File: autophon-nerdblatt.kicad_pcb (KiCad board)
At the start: 2 copper layers, 265 x 140 mm, 91 parts, among them J101 board-edge-connector, Q300 BSS84, Q301 BSS84, Q302 BSS84, Q303 BSS84, Q304 BSS84, Q305 BSS84, U101 LM1117-3.3, U102 LM2594M-5.0, U201 SN74LV1T34, U202 SN74LV1T34, U203 74AHCT595, U204 SN74LV1T34, U205 74AHCT595, U206 ESP32-WROOM-32, U207 74AHCT595, U300 L298HN, U301 L298HN, U302 L298HN

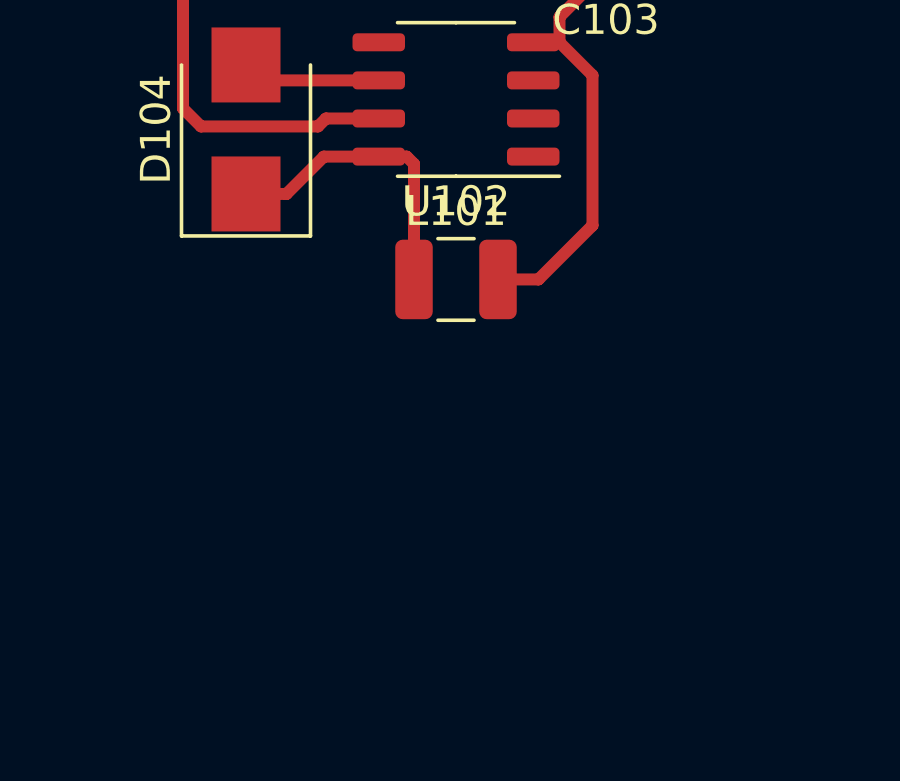
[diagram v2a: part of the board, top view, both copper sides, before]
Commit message: New Footprint for L
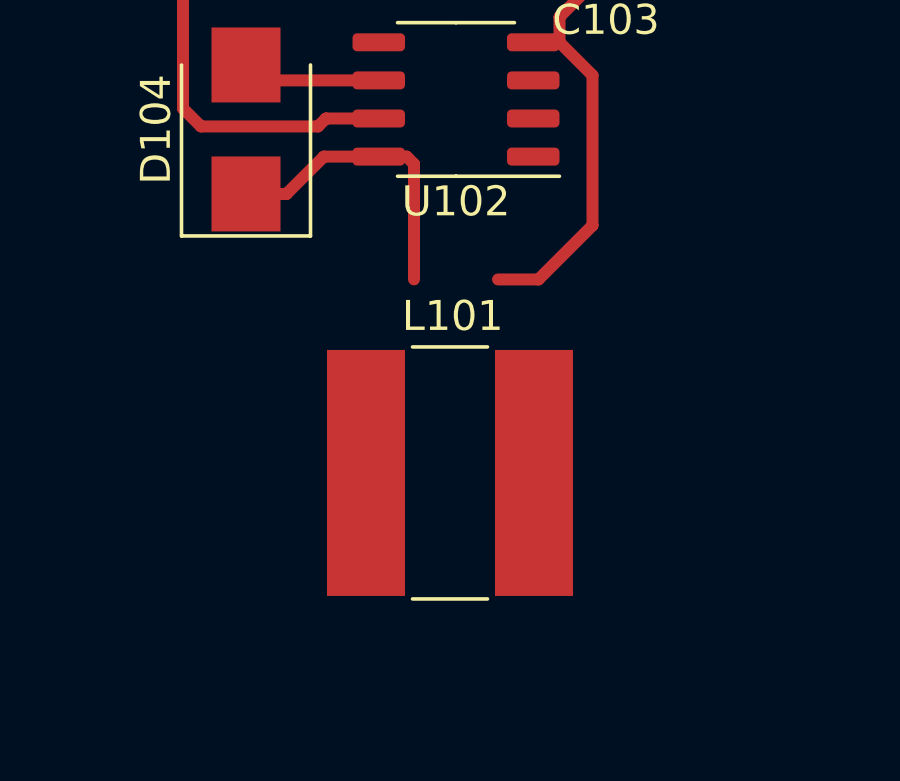
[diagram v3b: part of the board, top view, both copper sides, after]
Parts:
- L101: footprint Inductor_SMD:L_1210_3225Metric -> Inductor_SMD:L_Bourns-SRN8040_8x8.15mm
- moved L101 6.45 mm to (132.8, 108.5)

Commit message: more C vor Logic and placing first groups of parts
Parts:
- removed C201, C310: 100n, Capacitor_SMD:C_0603_1608Metric
- added C208: 1n, Capacitor_SMD:C_0603_1608Metric, F.Cu at (240.5, 101.4)
- added C209: 1n, Capacitor_SMD:C_0603_1608Metric, F.Cu at (222.3, 86.6)
- added C210: 1n, Capacitor_SMD:C_0603_1608Metric, F.Cu at (207.4, 85.8)
- added C211: 10n, Capacitor_SMD:C_0603_1608Metric, F.Cu at (268.2, 127.2)
- added C212: 10n, Capacitor_SMD:C_0603_1608Metric, F.Cu at (291.8, 127.2)
- added C213: 10n, Capacitor_SMD:C_0603_1608Metric, F.Cu at (212.7, 131.4)
- D201, D202, D300, D301, D302, D303, D304, D305: footprint Diode_SMD:D_SMB_Handsoldering -> Diode_SMD:D_SOT-23_ANK
- moved D301 151.7 mm to (195.3, 115.3), turned to -90 degrees
- moved C301 149.6 mm to (195.0, 117.9)
- moved R305 143.4 mm to (198.2, 117.9), turned to 180 degrees
- moved C300 142.9 mm to (195.4, 110.7)
- moved Q301 141.9 mm to (201.6, 118.5)
- moved D300 141.9 mm to (195.8, 108.2), turned to -90 degrees
- moved R303 141.7 mm to (198.2, 119.5)
- moved TP103 141.4 mm to (166.2, 118.5)
- moved R304 141.0 mm to (204.2, 118.2), turned to 90 degrees
- moved R300 138.6 mm to (198.5, 112.3)
- moved TP102 138.0 mm to (165.6, 111.6)
- moved C203 136.5 mm to (200.9, 88.4), turned to -90 degrees
- moved TP101 135.0 mm to (165.4, 103.8)
- moved R302 133.5 mm to (198.5, 110.7), turned to 180 degrees
- moved Q300 132.8 mm to (201.9, 111.2)
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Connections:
- net /ESP32_Shiftregs/HALL_INDEX_3V renamed HALL_INDEX_3V
- net /ESP32_Shiftregs/HALL_ROTOR_3V renamed HALL_ROTOR_3V
- net /ESP32_Shiftregs/MOT_EN_3V renamed MOT_EN_3V
- net /ESP32_Shiftregs/~HALL_EN_3V~ renamed ~HALL_EN_3V~
- net Net-(U206-Pad14) renamed SPI_CIPO
- C101 pad 2: GND -> ABCDEF_HALL_GND
- C102 pad 2: GND -> ABCDEF_HALL_GND
- C103 pad 2: GND -> ABCDEF_HALL_GND
- C104 pad 2: GND -> ABCDEF_HALL_GND
- C200 pad 2: GND -> ABCDEF_HALL_GND
- C202 pad 2: GND -> ABCDEF_HALL_GND
- C203 pad 2: GND -> ABCDEF_HALL_GND
- C204 pad 2: GND -> ABCDEF_HALL_GND
- C205 pad 2: GND -> ABCDEF_HALL_GND
- C206 pad 2: GND -> ABCDEF_HALL_GND
- C207 pad 2: GND -> ABCDEF_HALL_GND
- C300 pad 2: GND -> ABCDEF_HALL_GND
- C301 pad 2: GND -> ABCDEF_HALL_GND
- C302 pad 2: GND -> ABCDEF_HALL_GND
- C303 pad 2: GND -> ABCDEF_HALL_GND
- C304 pad 2: GND -> ABCDEF_HALL_GND
- C305 pad 2: GND -> ABCDEF_HALL_GND
- C306 pad 2: GND -> ABCDEF_HALL_GND
- C307 pad 2: GND -> ABCDEF_HALL_GND
- C308 pad 2: GND -> ABCDEF_HALL_GND
- C309 pad 2: GND -> ABCDEF_HALL_GND
- C311 pad 2: GND -> ABCDEF_HALL_GND
- C312 pad 2: GND -> ABCDEF_HALL_GND
- C313 pad 2: GND -> ABCDEF_HALL_GND
- C314 pad 2: GND -> ABCDEF_HALL_GND
- C315 pad 2: GND -> ABCDEF_HALL_GND
- D104 pad 2: GND -> ABCDEF_HALL_GND
- D201 pad 2: GND -> ABCDEF_HALL_GND
- D202 pad 2: GND -> ABCDEF_HALL_GND
- D300 pad 2: GND -> ABCDEF_HALL_GND
- D301 pad 2: GND -> ABCDEF_HALL_GND
- D302 pad 2: GND -> ABCDEF_HALL_GND
- D303 pad 2: GND -> ABCDEF_HALL_GND
- D304 pad 2: GND -> ABCDEF_HALL_GND
- D305 pad 2: GND -> ABCDEF_HALL_GND
- J101 pad 12A: no_connect_126 -> no_connect_105
- J101 pad 13A: no_connect_127 -> no_connect_106
- J101 pad 14A: no_connect_128 -> no_connect_107
- J101 pad 15A: no_connect_129 -> no_connect_108
- J101 pad 15B: no_connect_130 -> no_connect_109
- J101 pad 16A: no_connect_131 -> no_connect_110
- J101 pad 16B: no_connect_132 -> no_connect_111
- J101 pad 17A: no_connect_133 -> no_connect_112
- J101 pad 18A: no_connect_134 -> no_connect_113
- J101 pad 19A: no_connect_135 -> no_connect_114
- J101 pad 1A: no_connect_136 -> no_connect_115
- J101 pad 1B: no_connect_137 -> no_connect_116
- J101 pad 20A: no_connect_138 -> no_connect_117
- J101 pad 21A: no_connect_139 -> no_connect_118
- J101 pad 21B: no_connect_140 -> no_connect_119
- J101 pad 22A: no_connect_141 -> no_connect_120
- J101 pad 22B: no_connect_142 -> no_connect_121
- J101 pad 23B: no_connect_143 -> no_connect_122
- J101 pad 24B: no_connect_144 -> no_connect_123
- J101 pad 25B: no_connect_145 -> no_connect_124
- J101 pad 26A: no_connect_146 -> no_connect_125
- J101 pad 26B: no_connect_147 -> no_connect_126
- J101 pad 27B: no_connect_148 -> no_connect_127
- J101 pad 28B: no_connect_149 -> no_connect_128
- J101 pad 29B: no_connect_150 -> no_connect_129
- J101 pad 2A: no_connect_151 -> no_connect_130
- J101 pad 2B: no_connect_152 -> no_connect_131
- J101 pad 30A: no_connect_153 -> no_connect_132
- J101 pad 30B: no_connect_154 -> no_connect_133
- J101 pad 31B: no_connect_155 -> no_connect_134
- J101 pad 32B: no_connect_156 -> no_connect_135
- J101 pad 33B: no_connect_157 -> no_connect_136
- J101 pad 34A: no_connect_158 -> no_connect_137
- J101 pad 36B: no_connect_159 -> no_connect_138
- J101 pad 37A: F_MO_POS -> F_MOT_POS
- J101 pad 37B: GND -> ABCDEF_HALL_GND
- J101 pad 38A: no_connect_160 -> no_connect_139
- J101 pad 38B: no_connect_161 -> no_connect_140
- J101 pad 39A: no_connect_162 -> no_connect_141
- J101 pad 3A: no_connect_163 -> no_connect_142
- J101 pad 3B: no_connect_164 -> no_connect_143
- J101 pad 40A: no_connect_165 -> no_connect_144
- J101 pad 40B: no_connect_166 -> no_connect_145
- J101 pad 41A: no_connect_167 -> no_connect_146
- J101 pad 41B: no_connect_168 -> no_connect_147
- J101 pad 42A: no_connect_169 -> no_connect_148
- J101 pad 42B: no_connect_170 -> no_connect_149
- J101 pad 43A: no_connect_171 -> no_connect_150
- J101 pad 43B: no_connect_172 -> no_connect_151
- J101 pad 44A: no_connect_173 -> no_connect_152
- J101 pad 44B: no_connect_174 -> no_connect_153
- J101 pad 4A: no_connect_175 -> no_connect_154
- J101 pad 4B: no_connect_176 -> no_connect_155
- J101 pad 5A: no_connect_177 -> no_connect_156
- J101 pad 5B: no_connect_178 -> no_connect_157
- J101 pad 6B: no_connect_179 -> no_connect_158
- J101 pad 7A: no_connect_180 -> no_connect_159
- J101 pad 7B: no_connect_181 -> no_connect_160
- J101 pad 8A: GND -> ABCDEF_HALL_GND
- J101 pad 8B: no_connect_182 -> no_connect_161
- J101 pad 9A: no_connect_183 -> no_connect_162
- R202 pad 2: GND -> ABCDEF_HALL_GND
- R302 pad 2: GND -> ABCDEF_HALL_GND
- R305 pad 2: GND -> ABCDEF_HALL_GND
- R308 pad 2: GND -> ABCDEF_HALL_GND
- R311 pad 2: GND -> ABCDEF_HALL_GND
- R314 pad 2: GND -> ABCDEF_HALL_GND
- R317 pad 2: GND -> ABCDEF_HALL_GND
- U102 pad 1: GND -> ABCDEF_HALL_GND
- U102 pad 2: GND -> ABCDEF_HALL_GND
- U102 pad 3: GND -> ABCDEF_HALL_GND
- U102 pad 6: GND -> ABCDEF_HALL_GND
- U201 pad 3: GND -> ABCDEF_HALL_GND
- U202 pad 3: GND -> ABCDEF_HALL_GND
- U203 pad 1: /ESP32_Shiftregs/A_MOT_NEG_DRV -> A_MOT_NEG_DRV
- U203 pad 10: GND -> ABCDEF_HALL_GND
- U203 pad 11: /ESP32_Shiftregs/SPI_SCLK -> SPI_CLK
- U203 pad 12: /ESP32_Shiftregs/~SPI_CS0~ -> ~SPI_CSO~
- U203 pad 13: GND -> ABCDEF_HALL_GND
- U203 pad 14: /ESP32_Shiftregs/SPI_COPI -> SPI_COPI
- U203 pad 15: /ESP32_Shiftregs/A_MOT_POS_DRV -> A_MOT_POS_DRV
- U203 pad 2: /ESP32_Shiftregs/B_MOT_POS_DRV -> B_MOT_POS_DRV
- U203 pad 3: /ESP32_Shiftregs/B_MOT_NEG_DRV -> B_MOT_NEG_DRV
- U203 pad 4: /ESP32_Shiftregs/C_MOT_POS_DRV -> C_MOT_POS_DRV
- U203 pad 5: /ESP32_Shiftregs/C_MOT_NEG_DRV -> C_MOT_NEG_DRV
- U203 pad 6: /ESP32_Shiftregs/D_MOT_POS_DRV -> D_MOT_POS_DRV
- U203 pad 7: /ESP32_Shiftregs/D_MOT_NEG_DRV -> D_MOT_NEG_DRV
- U203 pad 8: GND -> ABCDEF_HALL_GND
- U204 pad 3: GND -> ABCDEF_HALL_GND
- U205 pad 1: /ESP32_Shiftregs/E_MOT_NEG_DRV -> E_MOT_NEG_DRV
- U205 pad 11: /ESP32_Shiftregs/SPI_SCLK -> SPI_CLK
- U205 pad 12: /ESP32_Shiftregs/~SPI_CS0~ -> ~SPI_CSO~
- U205 pad 13: GND -> ABCDEF_HALL_GND
- U205 pad 15: /ESP32_Shiftregs/E_MOT_POS_DRV -> E_MOT_POS_DRV
- U205 pad 2: /ESP32_Shiftregs/F_MOT_POS_DRV -> F_MOT_POS_DRV
- U205 pad 3: /ESP32_Shiftregs/F_MOT_NEG_DRV -> F_MOT_NEG_DRV
- U205 pad 8: GND -> ABCDEF_HALL_GND
- U206 pad 13: Net-(U206-Pad13) -> SPI_CLK
- U206 pad 16: Net-(U206-Pad16) -> SPI_COPI
- U206 pad 23: Net-(U206-Pad23) -> ~SPI_CSO~
- U206 pad 32: no_connect_184 -> no_connect_163
- U206 pad 6: /ESP32_Shiftregs/SPI_SCLK -> Net-(U206-Pad6)
- U206 pad 7: /ESP32_Shiftregs/~SPI_CS0~ -> Net-(U206-Pad7)
- U206 pad 9: /ESP32_Shiftregs/SPI_COPI -> Net-(U206-Pad9)
- U207 pad 1: /ESP32_Shiftregs/~B_HALL_PWR_EN~ -> ~B_HALL_PWR_EN~
- U207 pad 11: /ESP32_Shiftregs/SPI_SCLK -> SPI_CLK
- U207 pad 12: /ESP32_Shiftregs/~SPI_CS0~ -> ~SPI_CSO~
- U207 pad 15: /ESP32_Shiftregs/~A_HALL_PWR_EN~ -> ~A_HALL_PWR_EN~
- U207 pad 2: /ESP32_Shiftregs/~C_HALL_PWR_EN~ -> ~C_HALL_PWR_EN~
- U207 pad 3: /ESP32_Shiftregs/~D_HALL_PWR_EN~ -> ~D_HALL_PWR_EN~
- U207 pad 4: /ESP32_Shiftregs/~E_HALL_PWR_EN~ -> ~E_HALL_PWR_EN~
- U207 pad 5: Net-(U207-Pad5) -> ~F_HALL_PWR_EN~
- U207 pad 8: GND -> ABCDEF_HALL_GND
- U300 pad 1: GND -> ABCDEF_HALL_GND
- U300 pad 15: GND -> ABCDEF_HALL_GND
- U300 pad 8: GND -> ABCDEF_HALL_GND
- U301 pad 1: GND -> ABCDEF_HALL_GND
- U301 pad 15: GND -> ABCDEF_HALL_GND
- U301 pad 8: GND -> ABCDEF_HALL_GND
- U302 pad 1: GND -> ABCDEF_HALL_GND
- U302 pad 15: GND -> ABCDEF_HALL_GND
- U302 pad 8: GND -> ABCDEF_HALL_GND
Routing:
- net F_HALL_PWR: track 0.00 -> 41.5 mm
- net ~E_HALL_PWR_EN~: track 0.00 -> 40.2 mm
- net ~C_HALL_PWR_EN~: track 0.00 -> 35.9 mm
- net ~F_HALL_PWR_EN~: track 0.00 -> 34.7 mm
- net D_HALL_PWR: track 0.00 -> 32.9 mm
- net B_HALL_PWR: track 0.00 -> 27.7 mm
- net Net-(U205-Pad9): track 0.00 -> 26.7 mm
- net E_HALL_PWR: track 0.00 -> 25.4 mm
- net ~A_HALL_PWR_EN~: track 0.00 -> 24.6 mm
- net GND: track 24.3 -> 0.00 mm
- net ~D_HALL_PWR_EN~: track 0.00 -> 23.0 mm
- net ~B_HALL_PWR_EN~: track 0.00 -> 21.5 mm
- net A_HALL_PWR: track 0.00 -> 19.1 mm
- net C_HALL_PWR: track 0.00 -> 16.6 mm
- net +5V: track 18.2 -> 32.1 mm
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- added copper zone on F.Cu, net ABCDEF_HALL_GND
- removed copper zone on B.Cu, net GND
- removed copper zone on F.Cu, net GND

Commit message: first traces
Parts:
- moved D103 193.6 mm to (147.9, 107.7), turned to 90 degrees
- moved D101 192.3 mm to (144.6, 107.7), turned to 90 degrees
- moved R103 190.0 mm to (147.9, 104.5), turned to 90 degrees
- moved R101 187.0 mm to (144.6, 104.5), turned to -90 degrees
- moved R102 186.6 mm to (146.2, 104.5), turned to -90 degrees
- moved D102 185.1 mm to (146.2, 107.7), turned to 90 degrees
- moved C106 99.0 mm to (148.1, 90.8)
- moved C105 88.5 mm to (153.9, 99.5), turned to 0 degrees
- moved U101 72.8 mm to (154.5, 93.8)
- moved C107 55.1 mm to (217.5, 211.7), turned to 0 degrees
- moved TP101 45.9 mm to (120.6, 93.9)
- moved D201 37.5 mm to (235.8, 86.7), turned to 0 degrees
- moved C203 32.4 mm to (233.1, 85.2), turned to 90 degrees
- moved R201 32.3 mm to (233.1, 88.3), turned to 90 degrees
- moved C213 32.2 mm to (212.4, 99.2)
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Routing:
- net B_HALL_PWR: track 27.7 -> 63.5 mm
- net A_HALL_PWR: track 19.1 -> 52.3 mm
- net C_HALL_PWR: track 16.6 -> 49.7 mm
- net D_HALL_PWR: track 32.9 -> 62.9 mm
- net Net-(U205-Pad9): track 26.7 -> 0.00 mm
- net E_HALL_PWR: track 25.4 -> 48.6 mm
- net +5V: track 32.1 -> 54.8 mm
- net ABCDEF_HALL_ROTOR: track 7.54 -> 27.4 mm, vias 0 -> 1
- net F_HALL_PWR: track 41.5 -> 57.7 mm
- net HALL_INDEX_3V: track 0.00 -> 14.9 mm
- net ~A_HALL_PWR_EN~: track 24.6 -> 39.4 mm, vias 0 -> 4
- net VCC: track 3.60 -> 16.4 mm
- net ABCDEF_HALL_INDEX: track 7.00 -> 18.0 mm, vias 0 -> 1
- net ~C_HALL_PWR_EN~: track 35.9 -> 25.0 mm, vias 0 -> 2
- net HALL_ROTOR_3V: track 1.84 -> 8.41 mm
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
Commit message: GND-Plane on endge connector and BOT
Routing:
- net ABCDEF_HALL_GND: vias 0 -> 6
- added copper zone on B.Cu, net ABCDEF_HALL_GND

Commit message: all traces routed. ready for cleanup
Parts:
- removed C202, C204, C206, C207: 1n, Capacitor_SMD:C_0603_1608Metric
- added J1: Conn_01x06_Female, Connector_PinHeader_2.54mm:PinHeader_1x06_P2.54mm_Vertical, F.Cu at (160.8, 125.2)
- added R1: 10k, Resistor_SMD:R_0603_1608Metric, F.Cu at (176.7, 109.3)
- added R2: 10k, Resistor_SMD:R_0603_1608Metric, F.Cu at (200.4, 123.8)
- added SW1: SW_Push, autophon-nerdblatt:NAMAE_JTP-1138, F.Cu at (212.7, 123.9)
- added SW2: SW_Push, autophon-nerdblatt:NAMAE_JTP-1138, F.Cu at (169.1, 112.7)
- moved C107 91.1 mm to (203.3, 121.6)
- moved C200 90.3 mm to (200.4, 125.4)
- moved U206 90.1 mm to (188.6, 118.3)
- moved D101 33.1 mm to (119.0, 86.8)
- moved R101 33.1 mm to (119.0, 83.7)
- moved D103 19.2 mm to (144.3, 88.8), turned to -90 degrees
- moved R103 13.1 mm to (144.3, 92.0)
- moved C309 4.61 mm to (244.5, 95.0), turned to 180 degrees
- moved C211 2.87 mm to (266.2, 125.1)
- moved C212 2.76 mm to (289.8, 125.2)
- moved R204 1.88 mm to (216.6, 104.7), turned to 180 degrees
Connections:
- net HALL_INDEX_3V renamed /ESP32_Shiftregs/HALL_INDEX_3V
- net HALL_ROTOR_3V renamed /ESP32_Shiftregs/HALL_ROTOR_3V
- net MOT_EN_3V renamed /ESP32_Shiftregs/MOT_EN_3V
- net ~HALL_EN_3V~ renamed /ESP32_Shiftregs/~HALL_EN_3V~
- net ~SPI_CSO~ renamed /ESP32_Shiftregs/~SPI_CSO~
- C105 pad 2: Net-(C105-Pad2) -> ABCDEF_HALL_GND
- C106 pad 2: Net-(C105-Pad2) -> ABCDEF_HALL_GND
- C107 pad 2: Net-(C105-Pad2) -> ABCDEF_HALL_GND
- D101 pad 1: Net-(C105-Pad2) -> ABCDEF_HALL_GND
- D102 pad 1: Net-(C105-Pad2) -> ABCDEF_HALL_GND
- D103 pad 1: Net-(C105-Pad2) -> ABCDEF_HALL_GND
- J101 pad 12A: no_connect_105 -> no_connect_96
- J101 pad 13A: no_connect_106 -> no_connect_97
- J101 pad 14A: no_connect_107 -> no_connect_98
- J101 pad 15A: no_connect_108 -> no_connect_99
- J101 pad 15B: no_connect_109 -> no_connect_100
- J101 pad 16A: no_connect_110 -> no_connect_101
- J101 pad 16B: no_connect_111 -> no_connect_102
- J101 pad 17A: no_connect_112 -> no_connect_103
- J101 pad 18A: no_connect_113 -> no_connect_104
- J101 pad 19A: no_connect_114 -> no_connect_105
- J101 pad 1A: no_connect_115 -> no_connect_106
- J101 pad 1B: no_connect_116 -> no_connect_107
- J101 pad 20A: no_connect_117 -> no_connect_108
- J101 pad 21A: no_connect_118 -> no_connect_109
- J101 pad 21B: no_connect_119 -> no_connect_110
- J101 pad 22A: no_connect_120 -> no_connect_111
- J101 pad 22B: no_connect_121 -> no_connect_112
- J101 pad 23B: no_connect_122 -> no_connect_113
- J101 pad 24B: no_connect_123 -> no_connect_114
- J101 pad 25B: no_connect_124 -> no_connect_115
- J101 pad 26A: no_connect_125 -> no_connect_116
- J101 pad 26B: no_connect_126 -> no_connect_117
- J101 pad 27B: no_connect_127 -> no_connect_118
- J101 pad 28B: no_connect_128 -> no_connect_119
- J101 pad 29B: no_connect_129 -> no_connect_120
- J101 pad 2A: no_connect_130 -> no_connect_121
- J101 pad 2B: no_connect_131 -> no_connect_122
- J101 pad 30A: no_connect_132 -> no_connect_123
- J101 pad 30B: no_connect_133 -> no_connect_124
- J101 pad 31B: no_connect_134 -> no_connect_125
- J101 pad 32B: no_connect_135 -> no_connect_126
- J101 pad 33B: no_connect_136 -> no_connect_127
- J101 pad 34A: no_connect_137 -> no_connect_128
- J101 pad 36B: no_connect_138 -> no_connect_129
- J101 pad 38A: no_connect_139 -> no_connect_130
- J101 pad 38B: no_connect_140 -> no_connect_131
- J101 pad 39A: no_connect_141 -> no_connect_132
- J101 pad 3A: no_connect_142 -> no_connect_133
- J101 pad 3B: no_connect_143 -> no_connect_134
- J101 pad 40A: no_connect_144 -> no_connect_135
- J101 pad 40B: no_connect_145 -> no_connect_136
- J101 pad 41A: no_connect_146 -> no_connect_137
- J101 pad 41B: no_connect_147 -> no_connect_138
- J101 pad 42A: no_connect_148 -> no_connect_139
- J101 pad 42B: no_connect_149 -> no_connect_140
- J101 pad 43A: no_connect_150 -> no_connect_141
- J101 pad 43B: no_connect_151 -> no_connect_142
- J101 pad 44A: no_connect_152 -> no_connect_143
- J101 pad 44B: no_connect_153 -> no_connect_144
- J101 pad 4A: no_connect_154 -> no_connect_145
- J101 pad 4B: no_connect_155 -> no_connect_146
- J101 pad 5A: no_connect_156 -> no_connect_147
- J101 pad 5B: no_connect_157 -> no_connect_148
- J101 pad 6B: no_connect_158 -> no_connect_149
- J101 pad 7A: no_connect_159 -> no_connect_150
- J101 pad 7B: no_connect_160 -> no_connect_151
- J101 pad 8B: no_connect_161 -> no_connect_152
- J101 pad 9A: no_connect_162 -> no_connect_153
- U101 pad 1: Net-(C105-Pad2) -> ABCDEF_HALL_GND
- U206 pad 1: Net-(U206-Pad1) -> ABCDEF_HALL_GND
- U206 pad 15: Net-(U206-Pad1) -> ABCDEF_HALL_GND
- U206 pad 17: Net-(U206-Pad17) -> no_connect_154
- U206 pad 18: Net-(U206-Pad18) -> no_connect_155
- U206 pad 19: Net-(U206-Pad19) -> no_connect_156
- U206 pad 20: Net-(U206-Pad20) -> no_connect_157
- U206 pad 21: Net-(U206-Pad21) -> no_connect_158
- U206 pad 22: Net-(U206-Pad22) -> no_connect_159
- U206 pad 25: Net-(U206-Pad25) -> /ESP32_Shiftregs/ESP32_GPIO0
- U206 pad 3: Net-(U206-Pad3) -> /ESP32_Shiftregs/ESP32_EN
- U206 pad 32: no_connect_163 -> no_connect_160
- U206 pad 34: Net-(U206-Pad34) -> /ESP32_Shiftregs/ESP32_RX
- U206 pad 35: Net-(U206-Pad35) -> /ESP32_Shiftregs/ESP32_TX
- U206 pad 38: Net-(U206-Pad1) -> ABCDEF_HALL_GND
- U206 pad 39: Net-(U206-Pad1) -> ABCDEF_HALL_GND
- U206 pad 4: Net-(U206-Pad4) -> no_connect_161
- U206 pad 5: Net-(U206-Pad5) -> no_connect_162
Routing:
- net +5V: track 54.8 -> 343.1 mm, vias 0 -> 11
- net +24V: track 32.0 -> 264.3 mm, vias 0 -> 7
- net VCC: track 16.4 -> 224.7 mm, vias 0 -> 6
- net /ESP32_Shiftregs/~SPI_CSO~: track 0.00 -> 122.1 mm, vias 0 -> 5
- net SPI_CLK: track 0.00 -> 106.6 mm, vias 0 -> 6
- net GLOBAL_MOT_EN: track 1.88 -> 97.7 mm, vias 0 -> 1
- net Net-(U205-Pad9): track 0.00 -> 87.0 mm, vias 0 -> 4
- net SPI_COPI: track 0.00 -> 86.3 mm, vias 0 -> 2
- net /ESP32_Shiftregs/MOT_EN_3V: track 1.72 -> 60.4 mm, vias 0 -> 2
- net B_MOT_POS_DRV: track 0.00 -> 56.6 mm
- net B_MOT_NEG_DRV: track 0.00 -> 56.6 mm
- net A_MOT_NEG_DRV: track 0.00 -> 51.1 mm
- net /ESP32_Shiftregs/HALL_INDEX_3V: track 14.9 -> 63.2 mm, vias 0 -> 2
- net /ESP32_Shiftregs/ESP32_EN: track 0.00 -> 46.6 mm, vias 0 -> 3
- net A_MOT_POS_DRV: track 0.00 -> 44.4 mm
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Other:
- board size 265 x 140 mm -> 265 x 50.6 mm
